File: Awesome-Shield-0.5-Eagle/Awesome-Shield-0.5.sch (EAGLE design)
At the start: 13 parts, among them J1 ARDUINO_R3_SHIELDUNO_R3_SHIEL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, SW1 SPST_TACT-EVQQ2

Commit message: layout tweaks
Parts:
- removed R4, R5: (no value), rcl:R-EU_R1206
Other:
- moved on the sheet: F1, J1, LED1, Q1, R1, R2, R3, R6, R7, R8, SW1
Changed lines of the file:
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@@
 <setting verticaltext="up"/>
 </settings>
-<grid distance="0.1" unitdist="inch" unit="inch" style="lines" multiple="1" display="no" altdistance="0.01" altunitdist="inch" altunit="inch"/>
+<grid distance="0.1" unitdist="inch" unit="inch" style="dots" multiple="1" display="yes" altdistance="0.01" altunitdist="inch" altunit="inch"/>
 <layers>
 <layer number="1" name="Top" color="4" fill="1" visible="no" active="no"/>
@@
 <part name="R2" library="rcl" deviceset="R-EU_" device="R1206"/>
 <part name="R3" library="rcl" deviceset="R-EU_" device="R1206"/>
-<part name="R4" library="rcl" deviceset="R-EU_" device="R1206"/>
-<part name="R5" library="rcl" deviceset="R-EU_" device="R1206"/>
 <part name="R6" library="rcl" deviceset="R-EU_" device="R1206"/>
 <part name="R7" library="rcl" deviceset="R-EU_" device="R1206"/>
@@
 <part name="Q1" library="SparkFun-DiscreteSemi" deviceset="PHOTOTRANSISTOR" device="PT17-21C-L41-TR8"/>
 <part name="SW1" library="adafruit" deviceset="SPST_TACT" device="-EVQQ2"/>
+<part name="GND1" library="supply1" deviceset="GND" device=""/>
+<part name="GND2" library="supply1" deviceset="GND" device=""/>
+<part name="GND3" library="supply1" deviceset="GND" device=""/>
+<part name="GND4" library="supply1" deviceset="GND" device=""/>
+<part name="+3V1" library="supply1" deviceset="+3V3" device=""/>
+<part name="+3V2" library="supply1" deviceset="+3V3" device=""/>
+<part name="+3V3" library="supply1" deviceset="+3V3" device=""/>
+<part name="GND5" library="supply1" deviceset="GND" device=""/>
 </parts>
 <sheets>
@@
 <instances>
 <instance part="FRAME1" gate="G$1" x="0" y="0"/>
-<instance part="J1" gate="G$1" x="60.96" y="81.28"/>
-<instance part="LED1" gate="G$1" x="132.08" y="132.08"/>
-<instance part="R1" gate="G$1" x="111.76" y="137.16"/>
-<instance part="R2" gate="G$1" x="111.76" y="132.08"/>
-<instance part="R3" gate="G$1" x="111.76" y="127"/>
-<instance part="R4" gate="G$1" x="22.86" y="127"/>
-<instance part="R5" gate="G$1" x="147.32" y="78.74"/>
-<instance part="R6" gate="G$1" x="25.4" y="35.56"/>
-<instance part="R7" gate="G$1" x="96.52" y="35.56"/>
-<instance part="R8" gate="R?" x="127" y="78.74"/>
-<instance part="F1" gate="G$1" x="111.76" y="35.56"/>
-<instance part="Q1" gate="G$1" x="38.1" y="35.56"/>
-<instance part="SW1" gate="G$1" x="172.72" y="137.16"/>
+<instance part="J1" gate="G$1" x="220.98" y="129.54"/>
+<instance part="LED1" gate="G$1" x="299.72" y="134.62"/>
+<instance part="R1" gate="G$1" x="279.4" y="139.7"/>
+<instance part="R2" gate="G$1" x="279.4" y="134.62"/>
+<instance part="R3" gate="G$1" x="279.4" y="129.54"/>
+<instance part="R6" gate="G$1" x="213.36" y="208.28" rot="R270"/>
+<instance part="R7" gate="G$1" x="119.38" y="137.16" rot="R90"/>
+<instance part="R8" gate="R?" x="236.22" y="63.5" rot="R90"/>
+<instance part="F1" gate="G$1" x="119.38" y="116.84" rot="R90"/>
+<instance part="Q1" gate="G$1" x="210.82" y="190.5"/>
+<instance part="SW1" gate="G$1" x="294.64" y="208.28"/>
+<instance part="GND1" gate="1" x="312.42" y="119.38"/>
+<instance part="GND2" gate="1" x="213.36" y="175.26"/>
+<instance part="GND3" gate="1" x="119.38" y="99.06"/>
+<instance part="GND4" gate="1" x="236.22" y="45.72"/>
+<instance part="+3V1" gate="G$1" x="119.38" y="152.4"/>
+<instance part="+3V2" gate="G$1" x="236.22" y="81.28"/>
+<instance part="+3V3" gate="G$1" x="213.36" y="223.52"/>
+<instance part="GND5" gate="1" x="294.64" y="187.96"/>
 </instances>
 <busses>

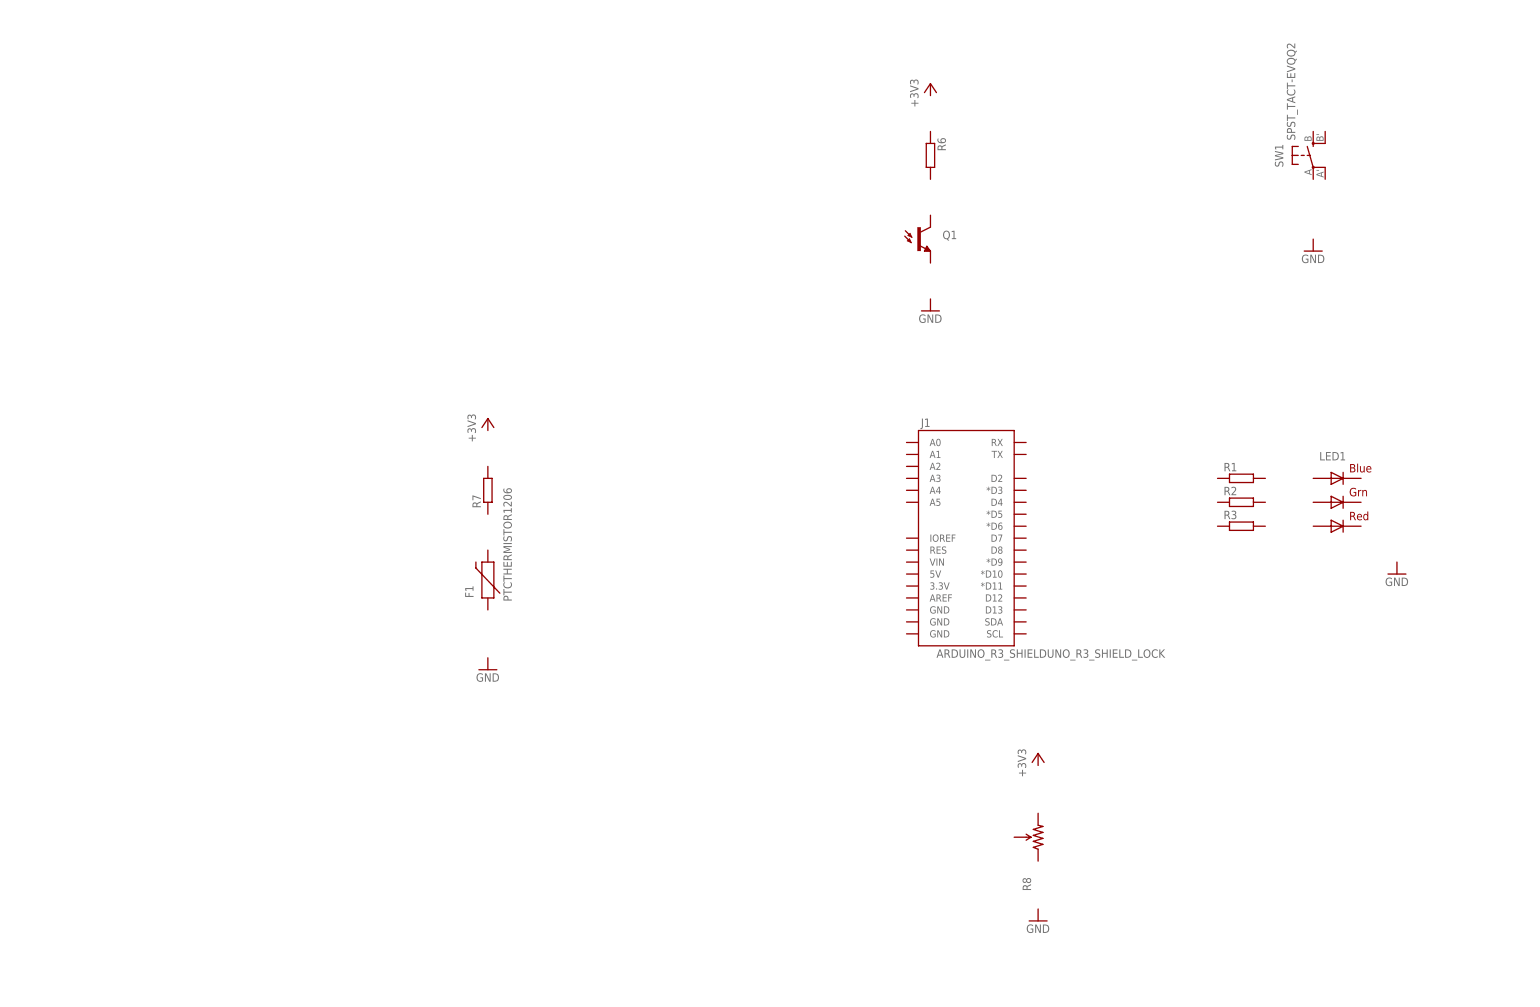
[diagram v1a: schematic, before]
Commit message: addded grove ports, began layout
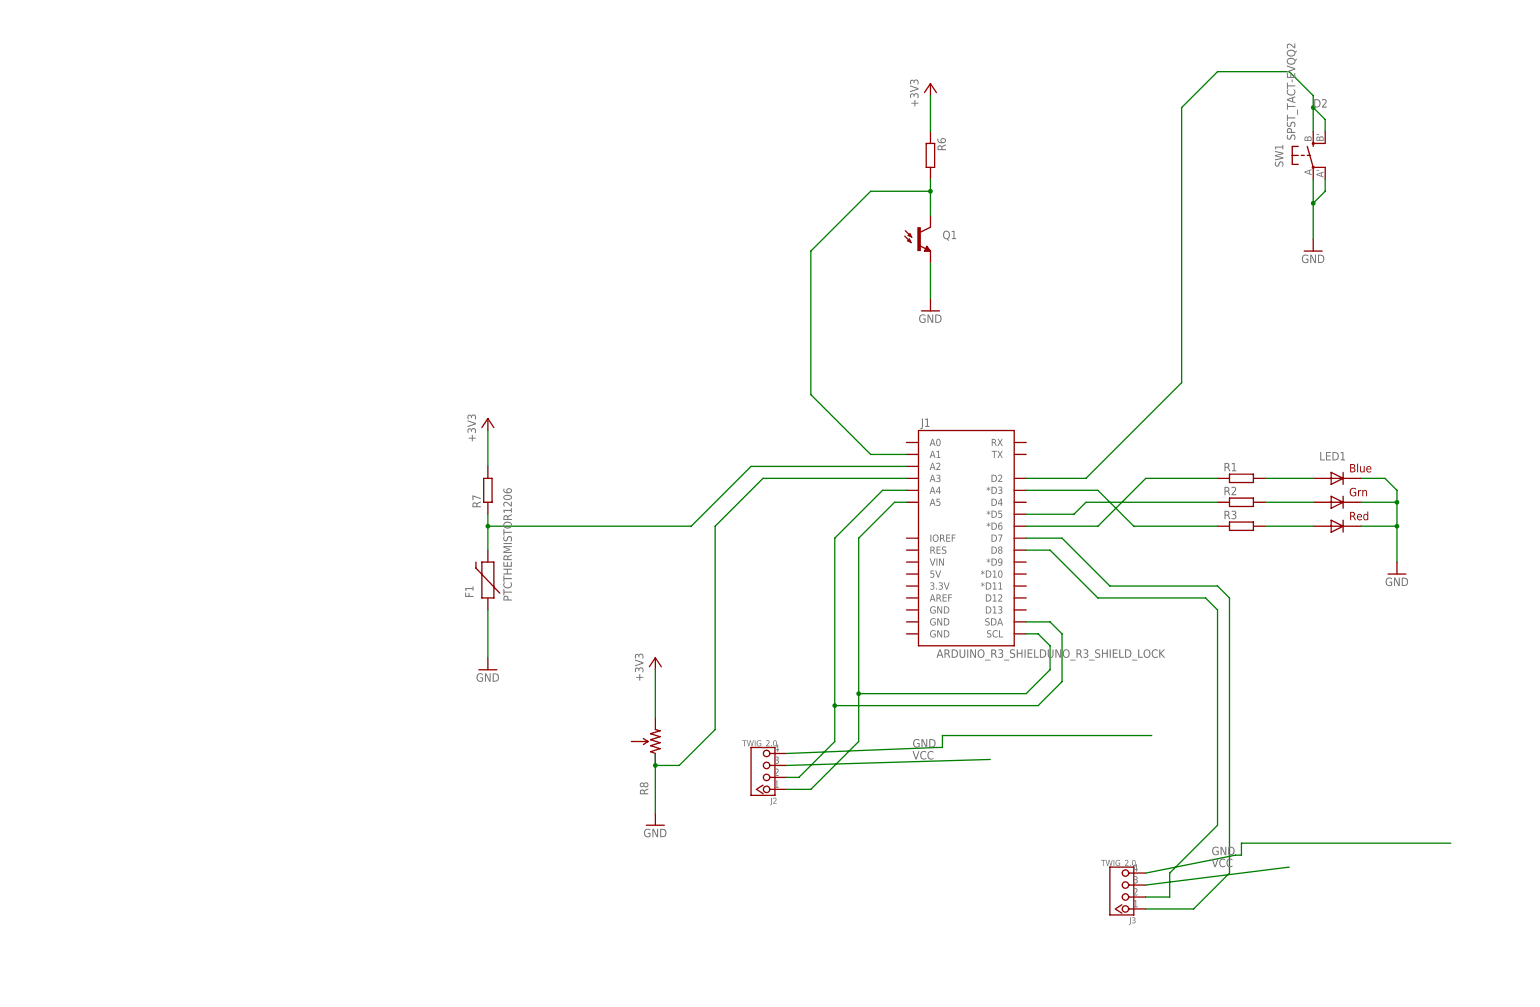
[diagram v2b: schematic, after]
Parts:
- added J2, J3: TWIG_2.0, CONNECTER:TWIG_2.0
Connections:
- new net +3V3: R6.1, R7.2, R8.CW
- new net D2: J1.D2, SW1.S, SW1.S1
- new net D3: J1.*D3, R3.1
- new net GND: F1.1, J1.A3, J2.4, J3.4, LED1.BLUE_C, LED1.GREEN_C, LED1.RED_C, Q1.E, R8.CCW, SW1.P, SW1.P1
- new net N$1: J1.A1, Q1.C, R6.2
- new net N$10: J1.D8, J3.2
- new net N$11: J1.D7, J3.1
- new net N$2: F1.2, J1.A2, R7.1
- new net N$3: LED1.RED_A, R3.2
- new net N$4: LED1.BLUE_A, R1.2
- new net N$5: LED1.GREEN_A, R2.2
- new net N$6: J1.A4, J1.SDA, J2.2
- new net N$7: J1.*D5, R2.1
- new net N$8: J1.*D6, R1.1
- new net N$9: J1.A5, J1.SCL, J2.1
- new net VCC: J2.3, J3.3
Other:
- moved on the sheet: R8

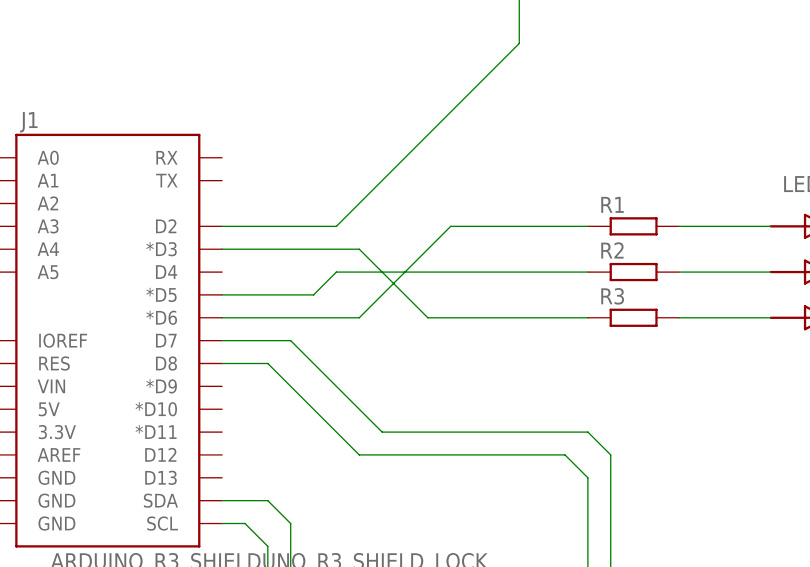
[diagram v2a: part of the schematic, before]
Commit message: swapped RGB LED pins to avoid crossing traces
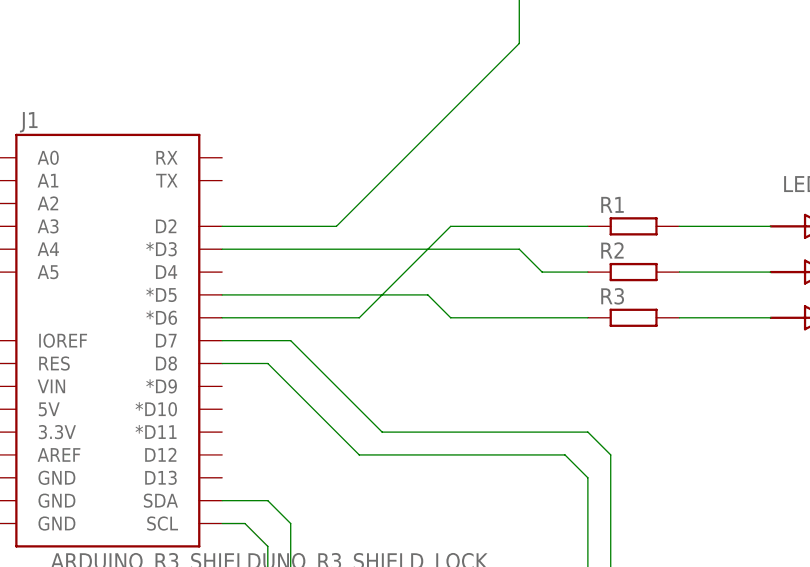
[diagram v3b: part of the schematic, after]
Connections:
- net D3: now also R2.1; no longer R3.1
- net N$7: now also R3.1; no longer R2.1
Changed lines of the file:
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@@
 <net name="D3" class="0">
 <segment>
-<pinref part="R3" gate="G$1" pin="1"/>
-<wire x1="274.32" y1="129.54" x2="256.54" y2="129.54" width="0.1524" layer="91"/>
-<wire x1="256.54" y1="129.54" x2="248.92" y2="137.16" width="0.1524" layer="91"/>
 <pinref part="J1" gate="G$1" pin="*D3"/>
-<wire x1="248.92" y1="137.16" x2="233.68" y2="137.16" width="0.1524" layer="91"/>
+<wire x1="233.68" y1="137.16" x2="266.7" y2="137.16" width="0.1524" layer="91"/>
+<wire x1="266.7" y1="137.16" x2="269.24" y2="134.62" width="0.1524" layer="91"/>
+<pinref part="R2" gate="G$1" pin="1"/>
+<wire x1="269.24" y1="134.62" x2="274.32" y2="134.62" width="0.1524" layer="91"/>
 </segment>
 </net>
 <net name="N$7" class="0">
 <segment>
-<pinref part="R2" gate="G$1" pin="1"/>
-<wire x1="274.32" y1="134.62" x2="246.38" y2="134.62" width="0.1524" layer="91"/>
-<wire x1="246.38" y1="134.62" x2="243.84" y2="132.08" width="0.1524" layer="91"/>
 <pinref part="J1" gate="G$1" pin="*D5"/>
-<wire x1="243.84" y1="132.08" x2="233.68" y2="132.08" width="0.1524" layer="91"/>
+<pinref part="R3" gate="G$1" pin="1"/>
+<wire x1="274.32" y1="129.54" x2="259.08" y2="129.54" width="0.1524" layer="91"/>
+<wire x1="259.08" y1="129.54" x2="256.54" y2="132.08" width="0.1524" layer="91"/>
+<wire x1="256.54" y1="132.08" x2="233.68" y2="132.08" width="0.1524" layer="91"/>
 </segment>
 </net>

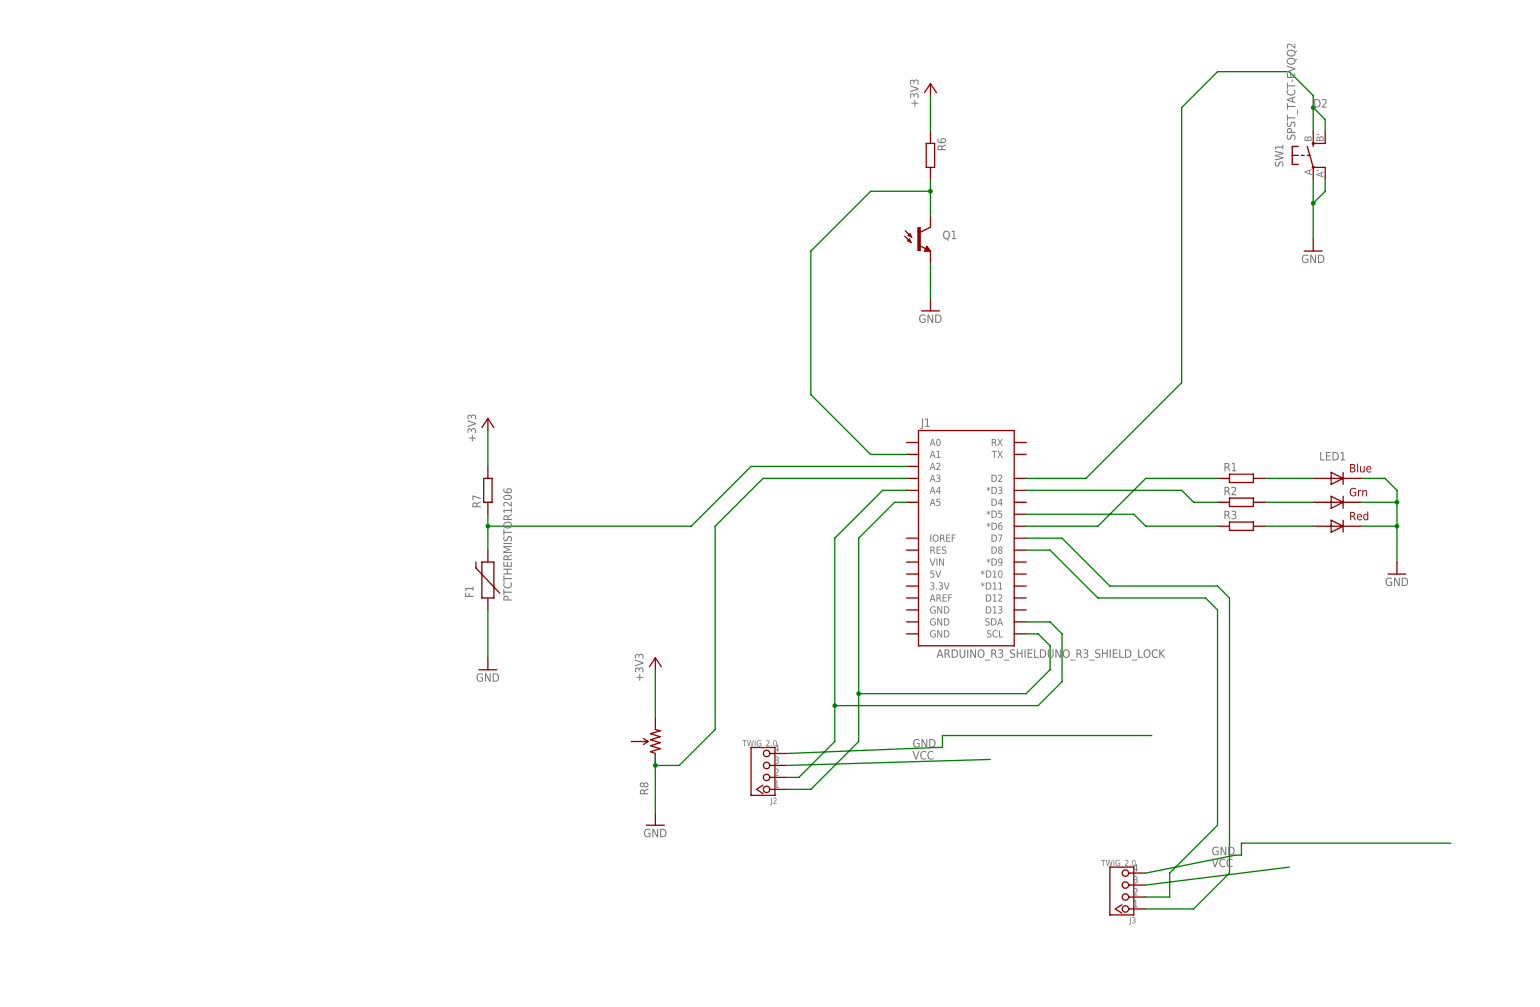
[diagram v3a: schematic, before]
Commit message: cleaned up schematics, reselected digital grove connector pins
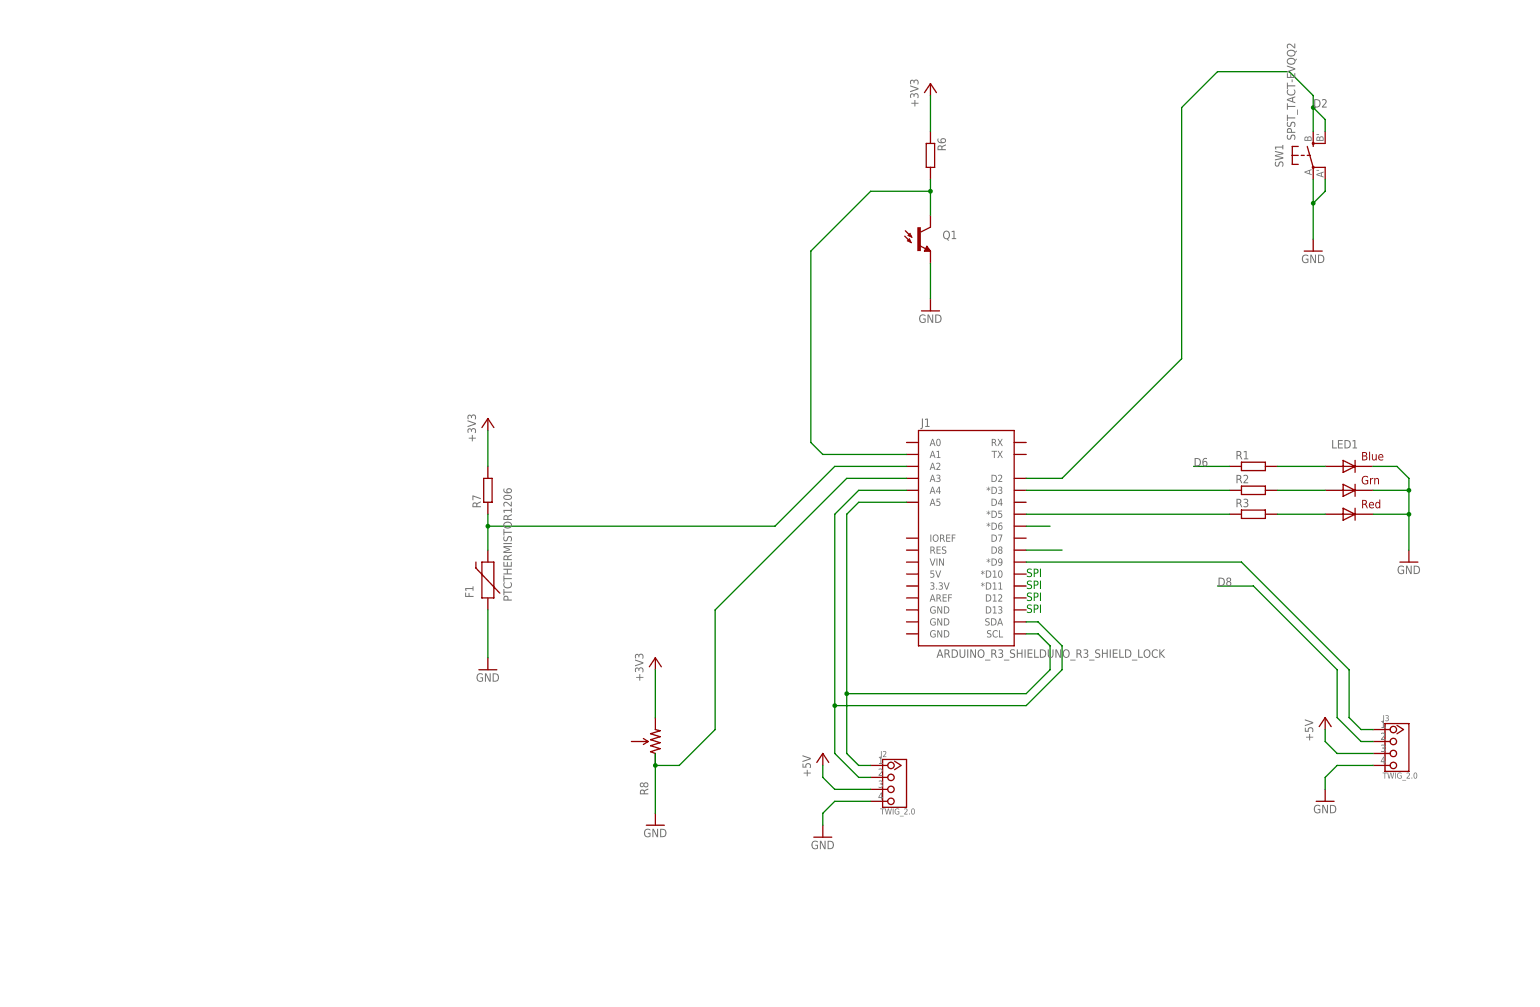
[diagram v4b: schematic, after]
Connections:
- net N$1 renamed A1
- net N$10 renamed D8
- net N$2 renamed A2
- net N$6 renamed A4
- net N$7 renamed D5
- net N$8 renamed D6
- net N$9 renamed A5
- net VCC renamed +5V
- removed net N$11: J1.D7, J3.1
- new net N$2: J1.*D9, J3.1
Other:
- note added: "SPI"
- moved on the sheet: J2, J3, LED1, R1, R2, R3
